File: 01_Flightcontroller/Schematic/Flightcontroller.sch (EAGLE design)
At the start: 89 parts, among them IC1 FT232RL, IC2 MPU6000, IC3 BMP280, J1 2908-05WB-MG, U1 STM32F7X2RXT, U2 ATMEGA328P_TQFP, U3 LM3940IMPX-3.3/NOPB, U4 TXB0104, Y1 8MHz, Y2 16MHz

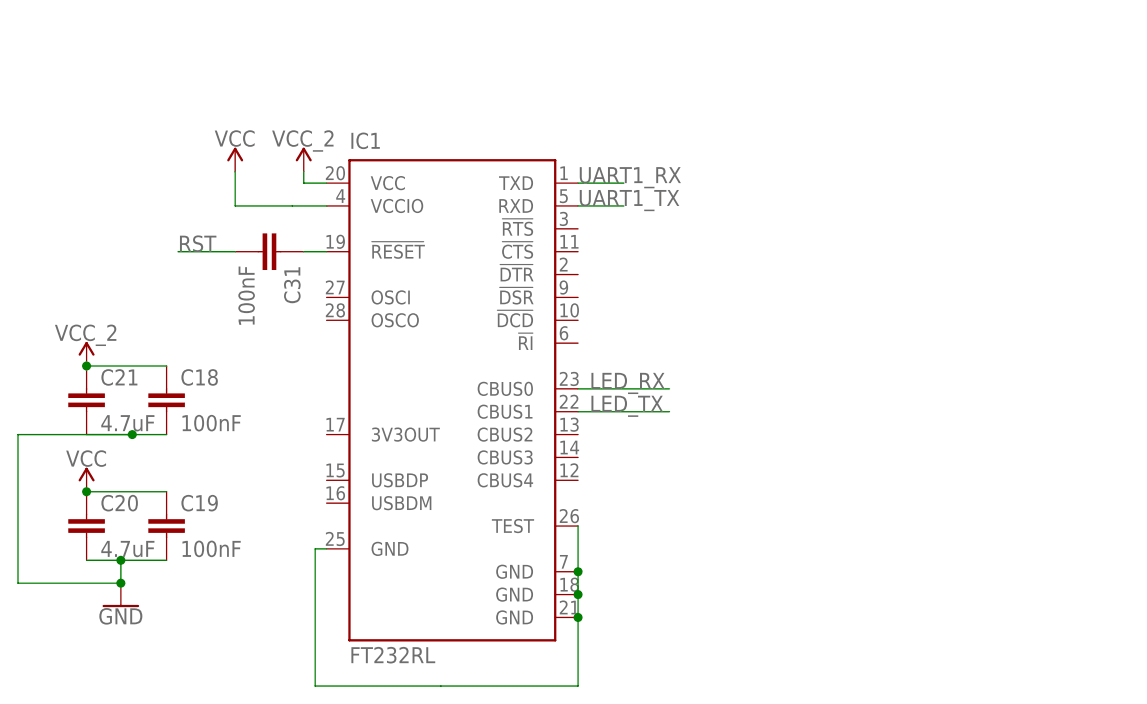
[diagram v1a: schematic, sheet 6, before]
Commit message: Hinzufügen USB , BATTSENS und VCC/GNDLAYER
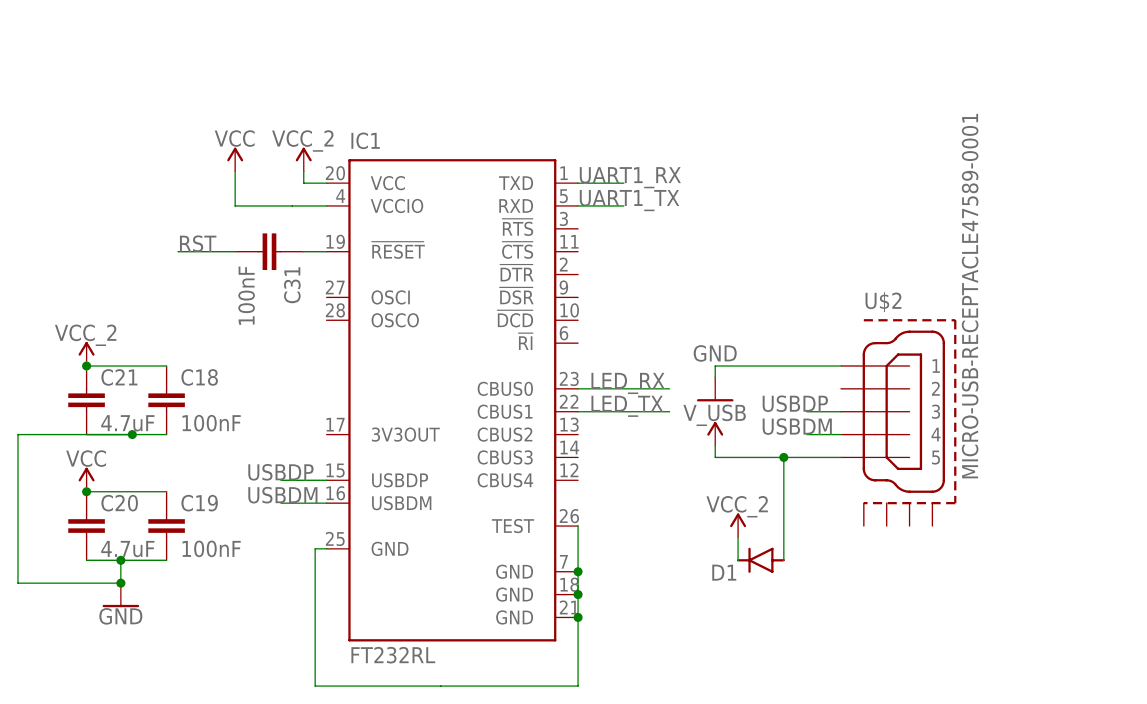
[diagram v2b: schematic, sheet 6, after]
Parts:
- added D1: (no value), diode:DIODE-DO214BA
- added JP10, JP8: (no value), adafruit:PINHD-1X1
- added JP9: (no value), adafruit:PINHD-1X3
- added U$2: MICRO-USB-RECEPTACLE47589-0001, con-molex-usb:MICRO-USB-RECEPTACLE47589-0001
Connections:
- new net USBDM: IC1.USBDM, U$2.4
- new net USBDP: IC1.USBDP, U$2.3
- new net V_USB: D1.A, U$2.5
- net BATTSENS: now also JP8.1
- net GND: now also JP10.1, JP9.3, U$2.1
- net USBOSD: now also JP9.2
- net VCC: now also JP9.1
- net VCC_2: now also D1.C
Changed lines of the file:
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@@
 <?xml version="1.0" encoding="utf-8"?>
 <!DOCTYPE eagle SYSTEM "eagle.dtd">
-<eagle version="9.1.3">
+<eagle version="9.3.2">
 <drawing>
 <settings>
@@
 <part name="JP7" library="adafruit" library_urn="urn:adsk.eagle:library:420" deviceset="PINHD-1X6" device="" package3d_urn="urn:adsk.eagle:package:6240711/1"/>
 <part name="SUPPLY21" library="SparkFun-PowerSymbols" library_urn="urn:adsk.eagle:library:530" deviceset="VCC_2" device=""/>
+<part name="U$2" library="con-molex-usb" deviceset="MICRO-USB-RECEPTACLE" device="47589-0001"/>
+<part name="SUPPLY33" library="SparkFun-PowerSymbols" library_urn="urn:adsk.eagle:library:530" deviceset="V_USB" device=""/>
+<part name="GND32" library="SparkFun-PowerSymbols" library_urn="urn:adsk.eagle:library:530" deviceset="GND" device=""/>
+<part name="SUPPLY34" library="SparkFun-PowerSymbols" library_urn="urn:adsk.eagle:library:530" deviceset="VCC" device=""/>
+<part name="GND33" library="SparkFun-PowerSymbols" library_urn="urn:adsk.eagle:library:530" deviceset="GND" device=""/>
+<part name="JP9" library="adafruit" library_urn="urn:adsk.eagle:library:420" deviceset="PINHD-1X3" device="" package3d_urn="urn:adsk.eagle:package:6240710/1"/>
+<part name="D1" library="diode" library_urn="urn:adsk.eagle:library:210" deviceset="DIODE-" device="DO214BA" package3d_urn="urn:adsk.eagle:package:43453/2"/>
+<part name="SUPPLY35" library="SparkFun-PowerSymbols" library_urn="urn:adsk.eagle:library:530" deviceset="VCC_2" device=""/>
+<part name="GND34" library="SparkFun-PowerSymbols" library_urn="urn:adsk.eagle:library:530" deviceset="GND" device=""/>
+<part name="JP8" library="adafruit" library_urn="urn:adsk.eagle:library:420" deviceset="PINHD-1X1" device="" package3d_urn="urn:adsk.eagle:package:6240654/1"/>
+<part name="JP10" library="adafruit" library_urn="urn:adsk.eagle:library:420" deviceset="PINHD-1X1" device="" package3d_urn="urn:adsk.eagle:package:6240654/1"/>
 </parts>
 <sheets>
@@
 <instance part="GND20" gate="1" x="76.2" y="20.32" smashed="yes">
 <attribute name="VALUE" x="76.2" y="20.066" size="1.778" layer="96" align="top-center"/>
+</instance>
+<instance part="GND34" gate="1" x="-40.64" y="48.26" smashed="yes">
+<attribute name="VALUE" x="-40.64" y="48.006" size="1.778" layer="96" align="top-center"/>
+</instance>
+<instance part="JP8" gate="G$1" x="-43.18" y="60.96" smashed="yes" rot="R180">
+<attribute name="NAME" x="-36.83" y="57.785" size="1.778" layer="95" rot="R180"/>
+<attribute name="VALUE" x="-36.83" y="66.04" size="1.778" layer="96" rot="R180"/>
+</instance>
+<instance part="JP10" gate="G$1" x="-43.18" y="55.88" smashed="yes" rot="R180">
+<attribute name="NAME" x="-36.83" y="52.705" size="1.778" layer="95" rot="R180"/>
+<attribute name="VALUE" x="-36.83" y="60.96" size="1.778" layer="96" rot="R180"/>
 </instance>
 </instances>
@@
 <pinref part="GND20" gate="1" pin="GND"/>
 <junction x="76.2" y="22.86"/>
+</segment>
+<segment>
+<pinref part="JP10" gate="G$1" pin="1"/>
+<pinref part="GND34" gate="1" pin="GND"/>
+<wire x1="-40.64" y1="55.88" x2="-40.64" y2="50.8" width="0.1524" layer="91"/>
 </segment>
 </net>
@@
 <segment>
 <pinref part="U1" gate="A" pin="PA6"/>
-<wire x1="7.62" y1="76.2" x2="3.81" y2="76.2" width="0.1524" layer="91"/>
 <label x="-5.08" y="76.2" size="1.778" layer="95"/>
+<wire x1="7.62" y1="76.2" x2="-17.78" y2="76.2" width="0.1524" layer="91"/>
+<wire x1="-17.78" y1="76.2" x2="-17.78" y2="60.96" width="0.1524" layer="91"/>
+<pinref part="JP8" gate="G$1" pin="1"/>
+<wire x1="-40.64" y1="60.96" x2="-17.78" y2="60.96" width="0.1524" layer="91"/>
 </segment>
 </net>
@@
 <instance part="SUPPLY21" gate="G$1" x="68.58" y="38.1" smashed="yes">
 <attribute name="VALUE" x="68.58" y="40.894" size="1.778" layer="96" align="bottom-center"/>
+</instance>
+<instance part="SUPPLY34" gate="G$1" x="114.3" y="25.4" smashed="yes">
+<attribute name="VALUE" x="114.3" y="28.194" size="1.778" layer="96" align="bottom-center"/>
+</instance>
+<instance part="GND33" gate="1" x="114.3" y="10.16" smashed="yes">
+<attribute name="VALUE" x="114.3" y="9.906" size="1.778" layer="96" align="top-center"/>
+</instance>
+<instance part="JP9" gate="A" x="140.97" y="19.05" smashed="yes">
+<attribute name="NAME" x="134.62" y="24.765" size="1.778" layer="95"/>
+<attribute name="VALUE" x="134.62" y="11.43" size="1.778" layer="96"/>
 </instance>
 </instances>
@@
 <pinref part="GND28" gate="1" pin="GND"/>
 </segment>
+<segment>
+<wire x1="114.3" y1="16.51" x2="114.3" y2="12.7" width="0.1524" layer="91"/>
+<pinref part="GND33" gate="1" pin="GND"/>
+<pinref part="JP9" gate="A" pin="3"/>
+<wire x1="114.3" y1="16.51" x2="138.43" y2="16.51" width="0.1524" layer="91"/>
+</segment>
 </net>
 <net name="VCC" class="1">
@@
 <wire x1="80.01" y1="7.62" x2="80.01" y2="12.7" width="0.1524" layer="91"/>
 <pinref part="SUPPLY30" gate="G$1" pin="VCC"/>
+</segment>
+<segment>
+<wire x1="114.3" y1="21.59" x2="114.3" y2="25.4" width="0.1524" layer="91"/>
+<pinref part="SUPPLY34" gate="G$1" pin="VCC"/>
+<pinref part="JP9" gate="A" pin="1"/>
+<wire x1="114.3" y1="21.59" x2="138.43" y2="21.59" width="0.1524" layer="91"/>
 </segment>
 </net>
@@
 </segment>
 </net>
+<net name="USBOSD" class="0">
+<segment>
+<label x="109.22" y="19.05" size="1.778" layer="95"/>
+<pinref part="JP9" gate="A" pin="2"/>
+<wire x1="114.3" y1="19.05" x2="138.43" y2="19.05" width="0.1524" layer="91"/>
+</segment>
+</net>
 </nets>
 </sheet>
@@
 <attribute name="NAME" x="49.911" y="64.516" size="1.778" layer="95" rot="R270"/>
 <attribute name="VALUE" x="44.831" y="64.516" size="1.778" layer="96" rot="R270"/>
+</instance>
+<instance part="U$2" gate="G$1" x="116.84" y="48.26" smashed="yes">
+<attribute name="NAME" x="114.3" y="59.69" size="1.778" layer="95" font="vector"/>
+<attribute name="VALUE" x="127" y="40.64" size="1.778" layer="96" font="vector" rot="R90"/>
+</instance>
+<instance part="SUPPLY33" gate="G$1" x="97.79" y="44.45" smashed="yes">
+<attribute name="VALUE" x="97.79" y="47.244" size="1.778" layer="96" align="bottom-center"/>
+</instance>
+<instance part="GND32" gate="1" x="97.79" y="49.53" smashed="yes">
+<attribute name="VALUE" x="97.79" y="55.626" size="1.778" layer="96" align="top-center"/>
+</instance>
+<instance part="D1" gate="G$1" x="102.87" y="31.75" smashed="yes" rot="R180">
+<attribute name="NAME" x="100.33" y="31.2674" size="1.778" layer="95" rot="R180"/>
+<attribute name="VALUE" x="100.33" y="34.0614" size="1.778" layer="96" rot="R180"/>
+</instance>
+<instance part="SUPPLY35" gate="G$1" x="100.33" y="34.29" smashed="yes">
+<attribute name="VALUE" x="100.33" y="37.084" size="1.778" layer="96" align="bottom-center"/>
 </instance>
 </instances>
@@
 <junction x="31.75" y="29.21"/>
 </segment>
+<segment>
+<pinref part="U$2" gate="G$1" pin="1"/>
+<wire x1="111.76" y1="53.34" x2="97.79" y2="53.34" width="0.1524" layer="91"/>
+<wire x1="97.79" y1="53.34" x2="97.79" y2="52.07" width="0.1524" layer="91"/>
+<pinref part="GND32" gate="1" pin="GND"/>
+</segment>
 </net>
 <net name="VCC" class="1">
@@
 <wire x1="36.83" y1="53.34" x2="27.94" y2="53.34" width="0.1524" layer="91"/>
 <junction x="27.94" y="53.34"/>
+</segment>
+<segment>
+<pinref part="D1" gate="G$1" pin="C"/>
+<wire x1="100.33" y1="31.75" x2="100.33" y2="34.29" width="0.1524" layer="91"/>
+<pinref part="SUPPLY35" gate="G$1" pin="VCC_2"/>
 </segment>
 </net>
@@
 </segment>
 </net>
+<net name="USBDP" class="0">
+<segment>
+<pinref part="IC1" gate="1" pin="USBDP"/>
+<wire x1="54.61" y1="40.64" x2="49.53" y2="40.64" width="0.1524" layer="91"/>
+<label x="45.72" y="40.64" size="1.778" layer="95"/>
+</segment>
+<segment>
+<pinref part="U$2" gate="G$1" pin="3"/>
+<wire x1="111.76" y1="48.26" x2="107.95" y2="48.26" width="0.1524" layer="91"/>
+<label x="102.87" y="48.26" size="1.778" layer="95"/>
+</segment>
+</net>
+<net name="USBDM" class="0">
+<segment>
+<pinref part="IC1" gate="1" pin="USBDM"/>
+<wire x1="54.61" y1="38.1" x2="49.53" y2="38.1" width="0.1524" layer="91"/>
+<label x="45.72" y="38.1" size="1.778" layer="95"/>
+</segment>
+<segment>
+<pinref part="U$2" gate="G$1" pin="4"/>
+<wire x1="111.76" y1="45.72" x2="107.95" y2="45.72" width="0.1524" layer="91"/>
+<label x="102.87" y="45.72" size="1.778" layer="95"/>
+</segment>
+</net>
+<net name="V_USB" class="1">
+<segment>
+<pinref part="U$2" gate="G$1" pin="5"/>
+<wire x1="111.76" y1="43.18" x2="105.41" y2="43.18" width="0.1524" layer="91"/>
+<wire x1="105.41" y1="43.18" x2="97.79" y2="43.18" width="0.1524" layer="91"/>
+<wire x1="97.79" y1="43.18" x2="97.79" y2="44.45" width="0.1524" layer="91"/>
+<pinref part="SUPPLY33" gate="G$1" pin="V_USB"/>
+<pinref part="D1" gate="G$1" pin="A"/>
+<wire x1="105.41" y1="43.18" x2="105.41" y2="31.75" width="0.1524" layer="91"/>
+<junction x="105.41" y="43.18"/>
+</segment>
+</net>

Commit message: Finnishing Board up. BOM
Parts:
- removed JP9: (no value), adafruit:PINHD-1X3
- removed U$2: MICRO-USB-RECEPTACLE47589-0001, con-molex-usb:MICRO-USB-RECEPTACLE47589-0001
- added DAC, OSD/USB: (no value), adafruit:PINHD-1X3
- added USB: (no value), SparkFun-Connectors:USB_MICRO-B_SMT
- C23: value 1uF -> 10uF
- renumbered IC1 to FT232RL, IC2 to MPU6000, IC3 to BMP280, ISP1 to ICSP, J1 to SD_CARD, JP10 to BATT_SENS, LED_STRIPES to LED, SW1 to RESET, U$1 to NRF24L01, U1 to STM32F722, U2 to ATMEGA328P, U3 to LM3940-3.3, U4 to TXB0104
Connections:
- net DAC_OUT: now also DAC.1
- net GND: now also DAC.3, OSD/USB.3, USB.GND, USB.SHIELD; no longer JP9.3, U$2.1
- net USBDM: now also USB.D-; no longer U$2.4
- net USBDP: now also USB.D+; no longer U$2.3
- net USBOSD: now also OSD/USB.2; no longer JP9.2
- net VCC: now also DAC.2, OSD/USB.1; no longer JP9.1
- net V_USB: now also USB.VBUS; no longer U$2.5
